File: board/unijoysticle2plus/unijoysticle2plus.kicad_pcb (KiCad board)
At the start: 2 copper layers, 34 parts, among them J1 DB9_Female, J2 DB9_Female, J3 Barrel_Jack, J4 Conn_01x03_Male, J5 USB_B_Micro, Q1 MMSS8050-H-TP, Q2 MMSS8050-H-TP, SW1 SW_Push, SW2 SW_SPST, SW3 SW_Push, SW4 SW_Push, U1 ESP32-WROOM-32D, U2 74LS05, U3 74LS05, U4 CH340C, U5 AP2114H-3_3TRG1

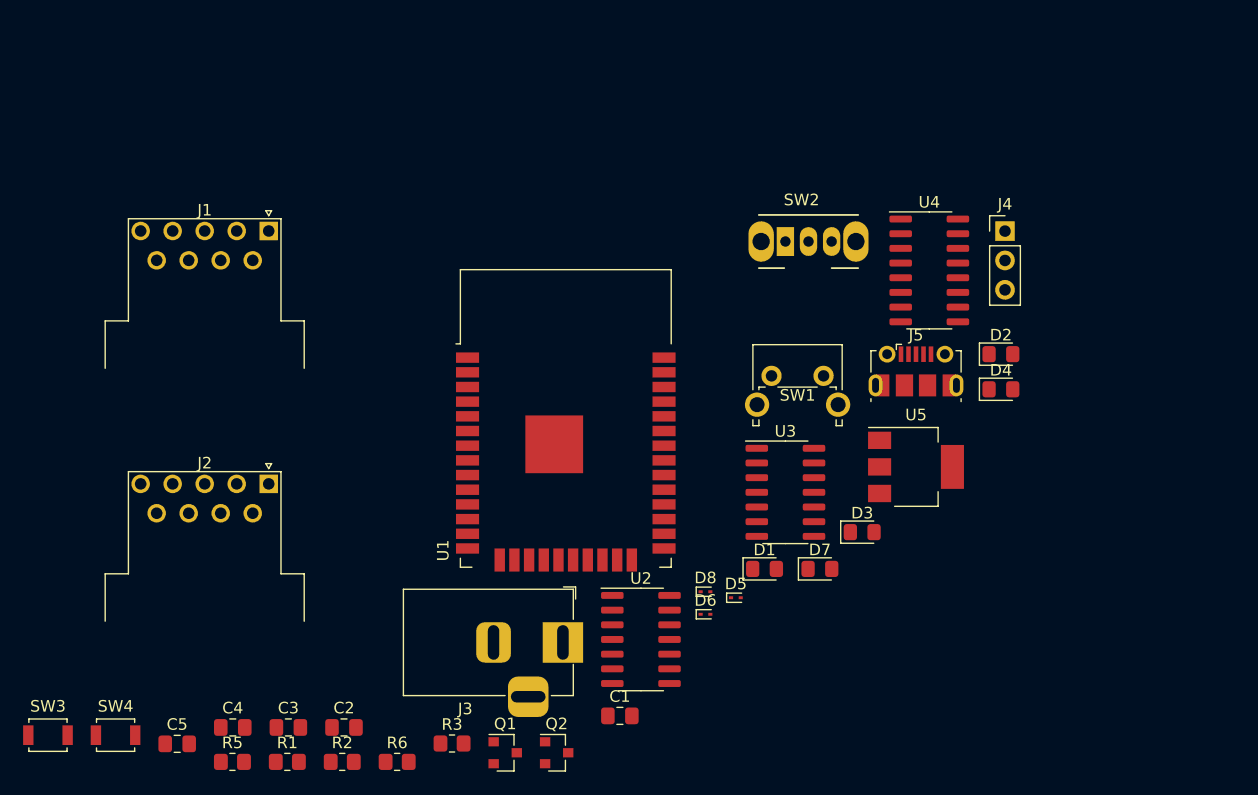
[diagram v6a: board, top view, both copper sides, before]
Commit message: unijoysticle2plus: use 0603 packges intead of 0805
LEDs, resistors and other components (where applicable) use 0603
packages intead of 0805. Smaller better.
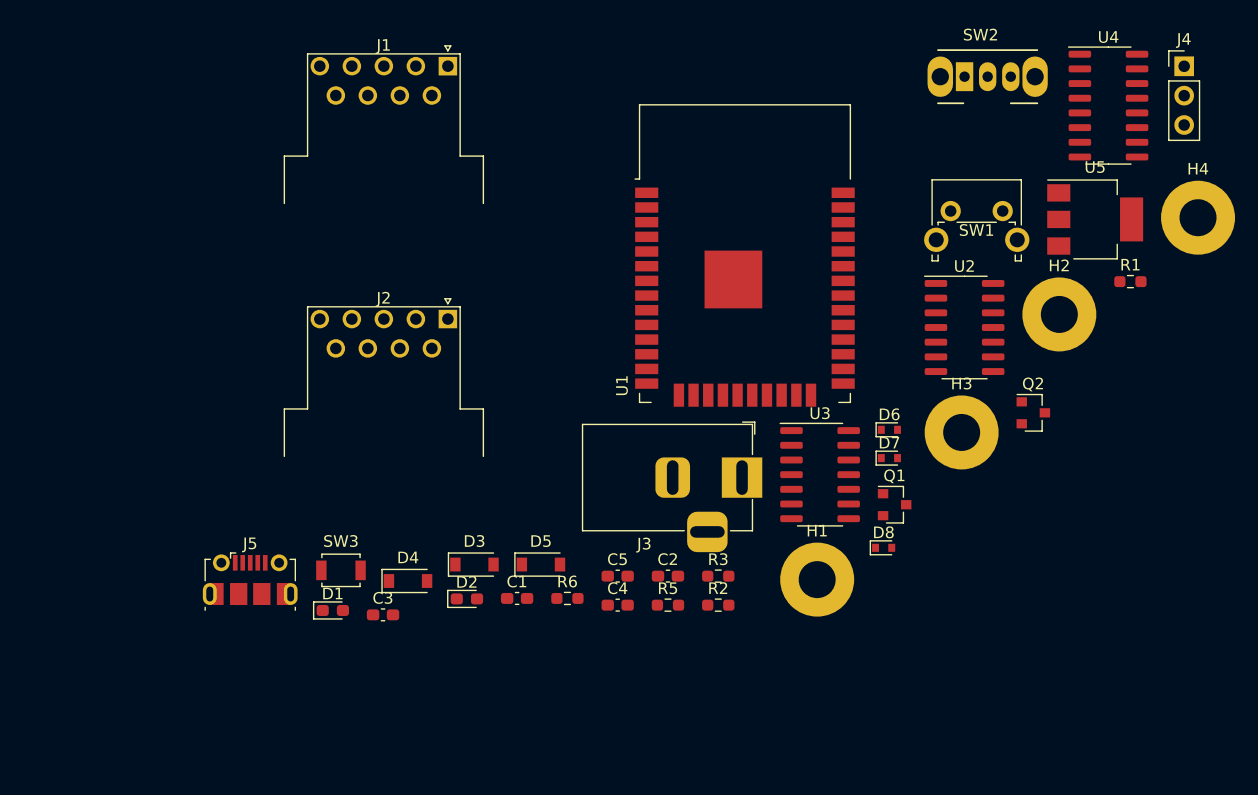
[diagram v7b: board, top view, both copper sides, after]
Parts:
- removed SW4: SW_Push, Button_Switch_SMD:SW_SPST_B3U-1000P
- added H1: MountingHole, MountingHole:MountingHole_3.2mm_M3_Pad, F.Cu at (153.0, 70.8)
- added H2: MountingHole, MountingHole:MountingHole_3.2mm_M3_Pad, F.Cu at (173.9, 47.8)
- added H3: MountingHole, MountingHole:MountingHole_3.2mm_M3_Pad, F.Cu at (165.5, 58.0)
- added H4: MountingHole, MountingHole:MountingHole_3.2mm_M3_Pad, F.Cu at (185.9, 39.5)
- C1, C2, C3, C4, C5: footprint Capacitor_SMD:C_0805_2012Metric_Pad1.18x1.45mm_HandSolder -> Capacitor_SMD:C_0603_1608Metric_Pad1.08x0.95mm_HandSolder
- D1, D2: footprint LED_SMD:LED_0805_2012Metric_Pad1.15x1.40mm_HandSolder -> LED_SMD:LED_0603_1608Metric_Pad1.05x0.95mm_HandSolder
- D3, D4: footprint Diode_SMD:D_0805_2012Metric_Pad1.15x1.40mm_HandSolder -> Diode_SMD:D_SOD-123
- D5: value ESD9B5.0ST5G -> 1N5819; footprint Diode_SMD:D_SOD-923 -> Diode_SMD:D_SOD-123
- D6, D8: value ESD9B5.0ST5G -> LESD5D5.0CT1G; footprint Diode_SMD:D_SOD-923 -> Diode_SMD:D_SOD-523
- D7: value 1N5819 -> LESD5D5.0CT1G; footprint Diode_SMD:D_0805_2012Metric_Pad1.15x1.40mm_HandSolder -> Diode_SMD:D_SOD-523
- R1, R2, R3, R5, R6: footprint Resistor_SMD:R_0805_2012Metric_Pad1.20x1.40mm_HandSolder -> Resistor_SMD:R_0603_1608Metric_Pad0.98x0.95mm_HandSolder
- U2, U3: value 74LS05 -> 74HC05
- moved R1 83.9 mm to (180.1, 45.0)
- moved J5 60.4 mm to (103.9, 70.8)
- moved D4 53.9 mm to (117.6, 70.9)
- moved D2 50.8 mm to (122.7, 72.4)
- moved Q2 50.7 mm to (171.7, 56.3)
- moved C5 40.8 mm to (135.7, 70.5)
- moved R5 40.0 mm to (140.1, 73.0)
- moved Q1 39.9 mm to (159.7, 64.3)
- moved U2 38.9 mm to (165.7, 49.0)
- moved D1 37.5 mm to (111.1, 73.4)
- moved R2 35.2 mm to (144.4, 73.0)
- moved C4 34.9 mm to (135.7, 73.0)
- moved D3 33.7 mm to (123.3, 69.5)
- moved C2 30.9 mm to (140.1, 70.5)
- moved SW3 29.1 mm to (111.8, 70.0)
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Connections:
- D6 pad 2: /USBD+ -> VBUS
- D7 pad 2: VBUS -> /USBD+
- U1 pad 25: Net-(SW4-Pad1) -> /ESP_BOOT

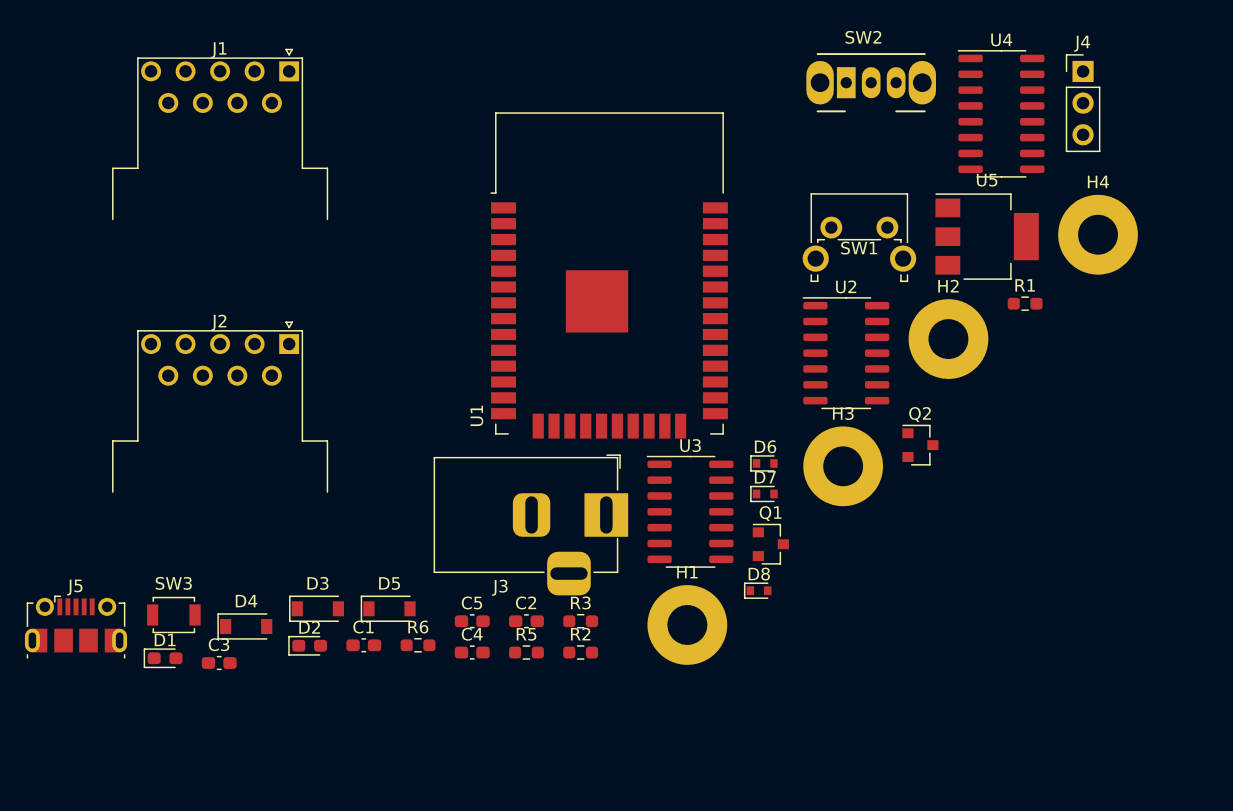
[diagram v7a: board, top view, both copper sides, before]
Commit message: unijoysticle2plus: cp2102, add extra 7405 and more
cp2102:
JLCPCB has the cp2102 as basic part. Cost wise, it might be a tiny bit
more expensive, but the footprint is smaller.
The downsize is that this is the cp2102, and not the recommended
cp2102N.

extra 74HC05:
Added another 74HC05 to connect POT-X, and POT-Y of Joy2. This could be
useful for Amiga computers, where some games (?) might use a 2nd and 3rd
buttons (?).

Add missing caps to ESP32, fixed some values, exposed GPIOs 36 and 39...
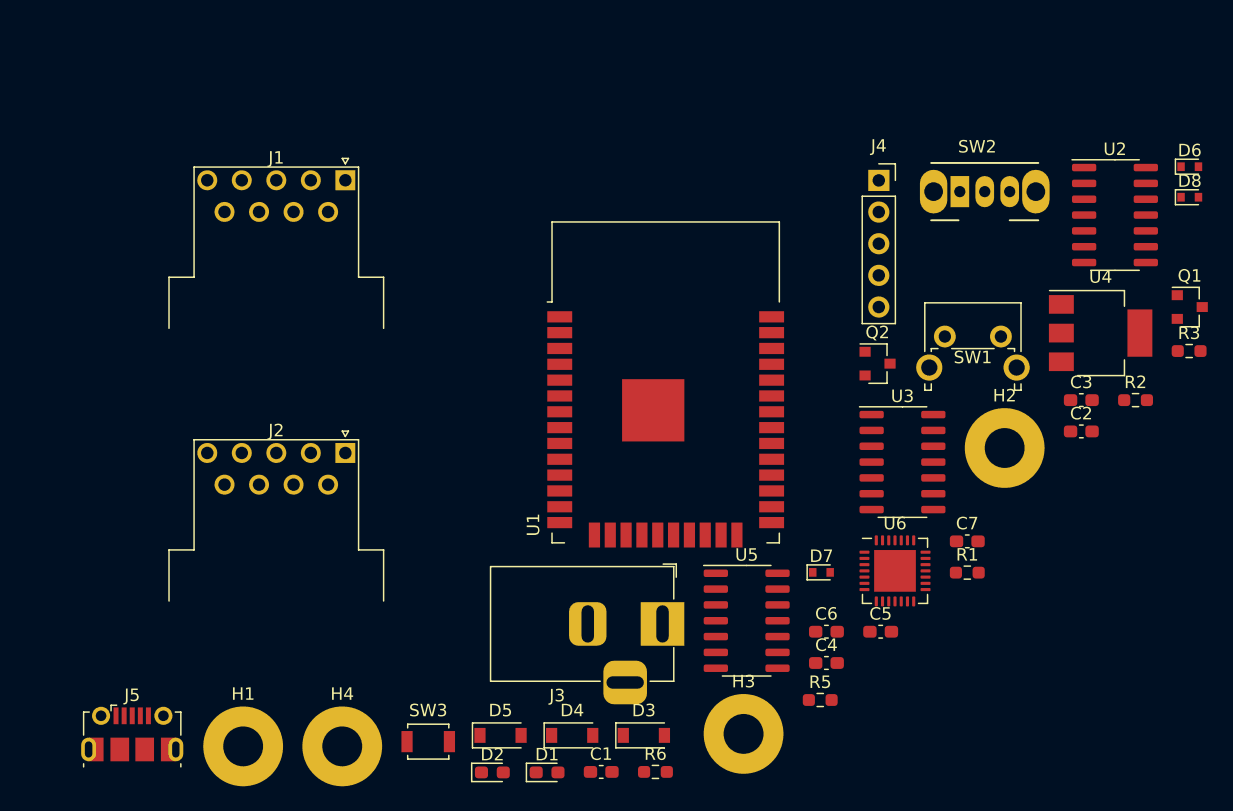
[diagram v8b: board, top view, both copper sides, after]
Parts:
- added C6: .1uF, Capacitor_SMD:C_0603_1608Metric_Pad1.08x0.95mm_HandSolder, F.Cu at (164.1, 71.3)
- added C7: 10uF, Capacitor_SMD:C_0603_1608Metric_Pad1.08x0.95mm_HandSolder, F.Cu at (175.4, 64.0)
- added U6: CP2102N-A01-GQFN28, Package_DFN_QFN:QFN-28-1EP_5x5mm_P0.5mm_EP3.35x3.35mm, F.Cu at (169.6, 66.4)
- C1, C3: value .1uF -> 4.7uF
- C4, C5: value 4.7uF -> 22uF
- J4: value Conn_01x03_Male -> Conn_01x05_Male; footprint Connector_PinHeader_2.54mm:PinHeader_1x03_P2.54mm_Vertical -> Connector_PinSocket_2.54mm:PinSocket_1x05_P2.54mm_Vertical
- Q1, Q2: value MMSS8050-H-TP -> MMSS8050
- U4: value CH340C -> AMS1117-3.3; footprint Package_SO:SOIC-16_3.9x9.9mm_P1.27mm -> Package_TO_SOT_SMD:SOT-223-3_TabPin2
- U5: value AP2114H-3_3TRG1 -> 74LS05; footprint Package_TO_SOT_SMD:SOT-223 -> Package_SO:SOIC-14_3.9x8.7mm_P1.27mm
- moved H4 73.2 mm to (125.3, 80.5)
- moved C3 72.3 mm to (184.6, 52.7)
- moved R3 53.4 mm to (193.2, 48.8)
- moved R2 48.9 mm to (188.9, 52.7)
- moved C2 47.1 mm to (184.6, 55.2)
- moved D8 46.8 mm to (193.3, 36.4)
- moved D6 41.6 mm to (193.3, 34.0)
- moved Q1 38.6 mm to (193.3, 45.2)
- moved H1 36.9 mm to (117.3, 80.5)
- moved U5 36.4 mm to (157.7, 70.4)
- moved C5 32.8 mm to (168.5, 71.3)
- moved D1 32.0 mm to (141.7, 82.6)
- moved C4 28.4 mm to (164.1, 73.8)
- moved D3 28.1 mm to (149.5, 79.6)
- moved D4 27.6 mm to (143.7, 79.6)
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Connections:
- net /ESP_RESET renamed /ESP_EN
- C1 pad 2: +5V -> GND
- C2 pad 1: Net-(C2-Pad1) -> +3V3
- C2 pad 2: +5V -> GND
- C3 pad 1: +5V -> GND
- C3 pad 2: Net-(C3-Pad2) -> +3V3
- C4 pad 1: +5V -> Net-(C4-Pad1)
- C4 pad 2: +5V -> GND
- C5 pad 2: +5V -> GND
- D1 pad 1: +5V -> GND
- D2 pad 1: +5V -> GND
- D3 pad 1: +5V -> Net-(C4-Pad1)
- D3 pad 2: Net-(D3-Pad2) -> VBUS
- D5 pad 1: +5V -> Net-(C4-Pad1)
- D5 pad 2: VBUS -> +5V
- D6 pad 1: +5V -> GND
- D7 pad 1: +5V -> GND
- D8 pad 1: +5V -> GND
- J1 pad 8: +5V -> GND
- J2 pad 8: +5V -> GND
- J3 pad 1: Net-(D3-Pad2) -> +5V
- J3 pad 2: +5V -> GND
- J5 pad 5: +5V -> GND
- J5 pad 6: +5V -> GND
- SW1 pad 1: +5V -> GND
- SW3 pad 1: +5V -> GND
- U1 pad 1: +5V -> GND
- U1 pad 15: +5V -> GND
- U1 pad 38: +5V -> GND
- U1 pad 39: +5V -> GND
- U1 pad 4: Net-(U1-Pad4) -> /GPIO36
- U1 pad 5: Net-(U1-Pad5) -> /GPIO39
- U2 pad 12: Net-(U2-Pad12) -> /J1_POTX
- U2 pad 13: Net-(U2-Pad13) -> /GPIO_J1_POTX
- U2 pad 7: +5V -> GND
- U3 pad 12: Net-(U3-Pad12) -> /J1_POTY
- U3 pad 13: Net-(U3-Pad13) -> /GPIO_J1_POTY
- U3 pad 7: +5V -> GND
- U4 pad 1: +5V -> GND
- U4 pad 2: /ESP_RXD -> +3V3
- U4 pad 3: /ESP_TXD -> Net-(C4-Pad1)
- U5 pad 1: +5V -> /GPIO_J2_POTX
- U5 pad 2: +3V3 -> /J2_POTX
- U5 pad 3: +5V -> /GPIO_J2_POTY
- U5 pad 4: +3V3 -> /J2_POTY
